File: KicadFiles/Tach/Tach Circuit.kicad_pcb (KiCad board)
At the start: 2 copper layers, 15 parts, among them Q1 2N3904

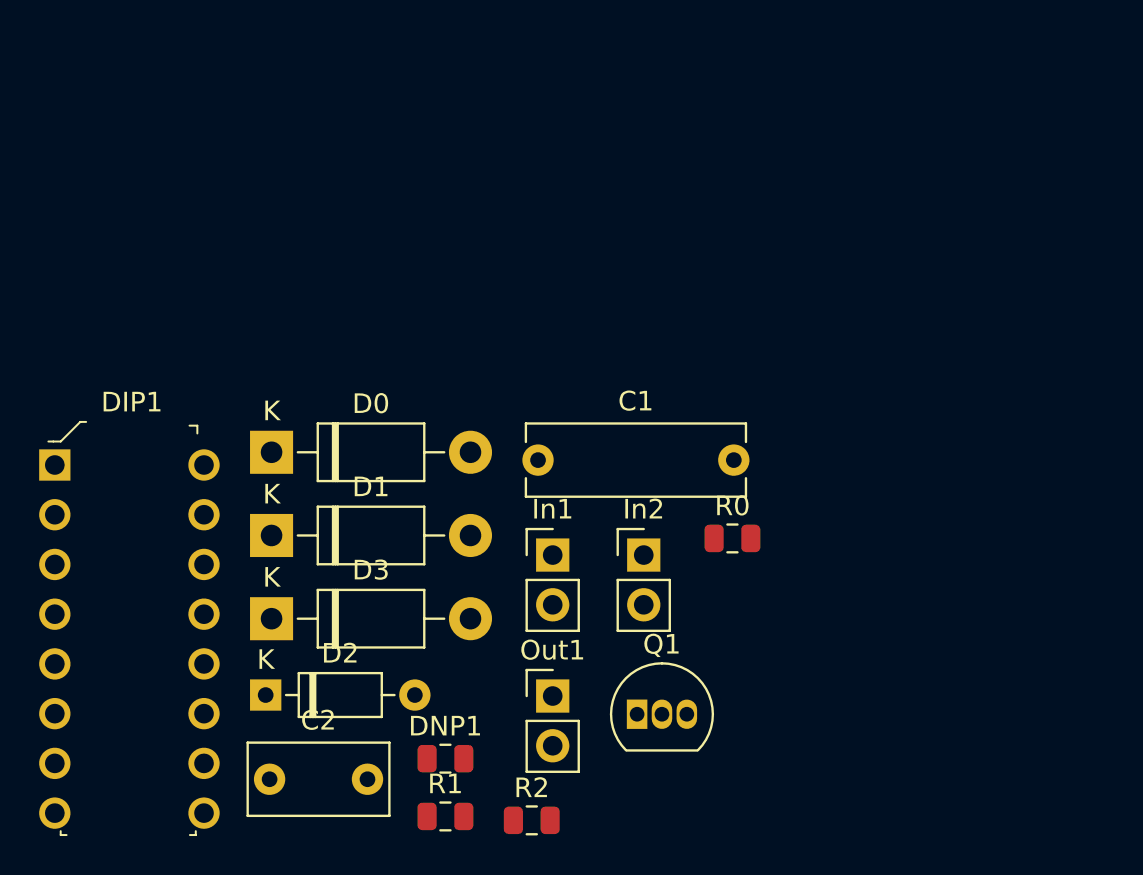
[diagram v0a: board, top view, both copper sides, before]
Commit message: ground = poured
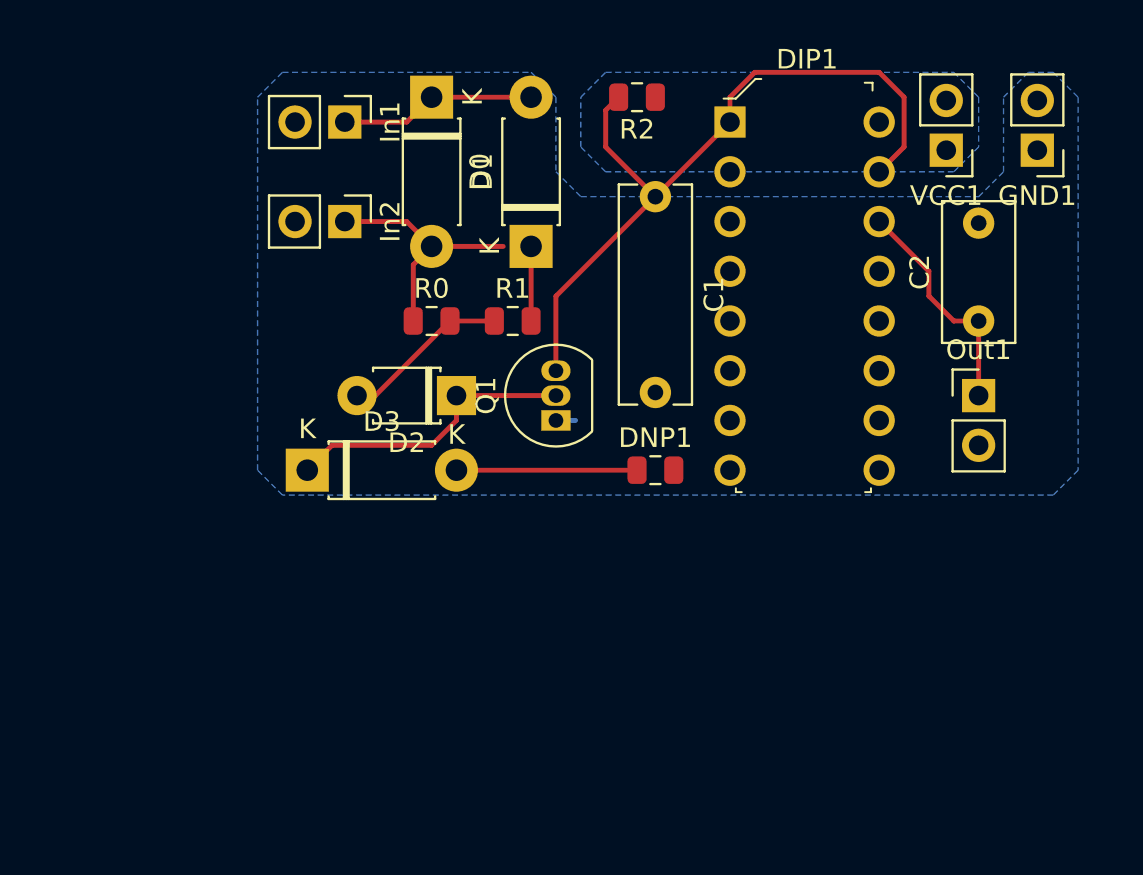
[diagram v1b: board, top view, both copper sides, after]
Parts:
- added GND1: GND, Connector_PinHeader_2.54mm:PinHeader_1x02_P2.54mm_Vertical, F.Cu at (164.3, -101.4)
- added VCC1: 5V, Connector_PinHeader_2.54mm:PinHeader_1x02_P2.54mm_Vertical, F.Cu at (159.6, -101.4)
- D0, D1, D3: footprint Diode_THT:D_DO-41_SOD81_P10.16mm_Horizontal -> Diode_THT:D_DO-41_SOD81_P7.62mm_Horizontal
- D2: footprint Diode_THT:D_DO-35_SOD27_P7.62mm_Horizontal -> Diode_THT:D_T-1_P5.08mm_Horizontal
- moved C2 43.1 mm to (161.3, -92.7), turned to 90 degrees
- moved DIP1 38.7 mm to (148.6, -102.9)
- moved R2 37.3 mm to (143.8, -104.1), turned to 180 degrees
- moved Out1 26.6 mm to (161.3, -88.9)
- moved R1 25.5 mm to (137.5, -92.7)
- moved In1 24.5 mm to (128.9, -102.9), turned to 270 degrees
- moved In2 22.9 mm to (128.9, -97.8), turned to 270 degrees
- moved D0 19.9 mm to (133.3, -104.1), turned to 270 degrees
- moved D1 19.8 mm to (138.4, -96.5), turned to 90 degrees
- moved R0 19.0 mm to (133.3, -92.7)
- moved DNP1 18.2 mm to (144.8, -85.1)
- moved D2 18.1 mm to (134.6, -88.9), turned to 180 degrees
- moved Q1 15.6 mm to (139.7, -87.6), turned to 90 degrees
- moved C1 14.7 mm to (144.8, -99.1), turned to 270 degrees
- moved D3 7.80 mm to (127.0, -85.1)
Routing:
- net Net-(C1-Pad1): track 0.00 -> 38.3 mm
- net Net-(D2-Pad1): track 0.00 -> 15.0 mm
- net Net-(D0-Pad2): track 0.00 -> 12.8 mm
- net Net-(C2-Pad1): track 0.00 -> 11.7 mm
- net Net-(D0-Pad1): track 0.00 -> 10.0 mm
- net Net-(D3-Pad2): track 0.00 -> 9.22 mm
- net Net-(D2-Pad2): track 0.00 -> 8.59 mm
- net Net-(D1-Pad1): track 0.00 -> 3.81 mm
- net GND: track 0.00 -> 1.37 mm
- added copper zone on B.Cu, net +5V
- added copper zone on B.Cu, net GND

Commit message: backdash footprints assigned
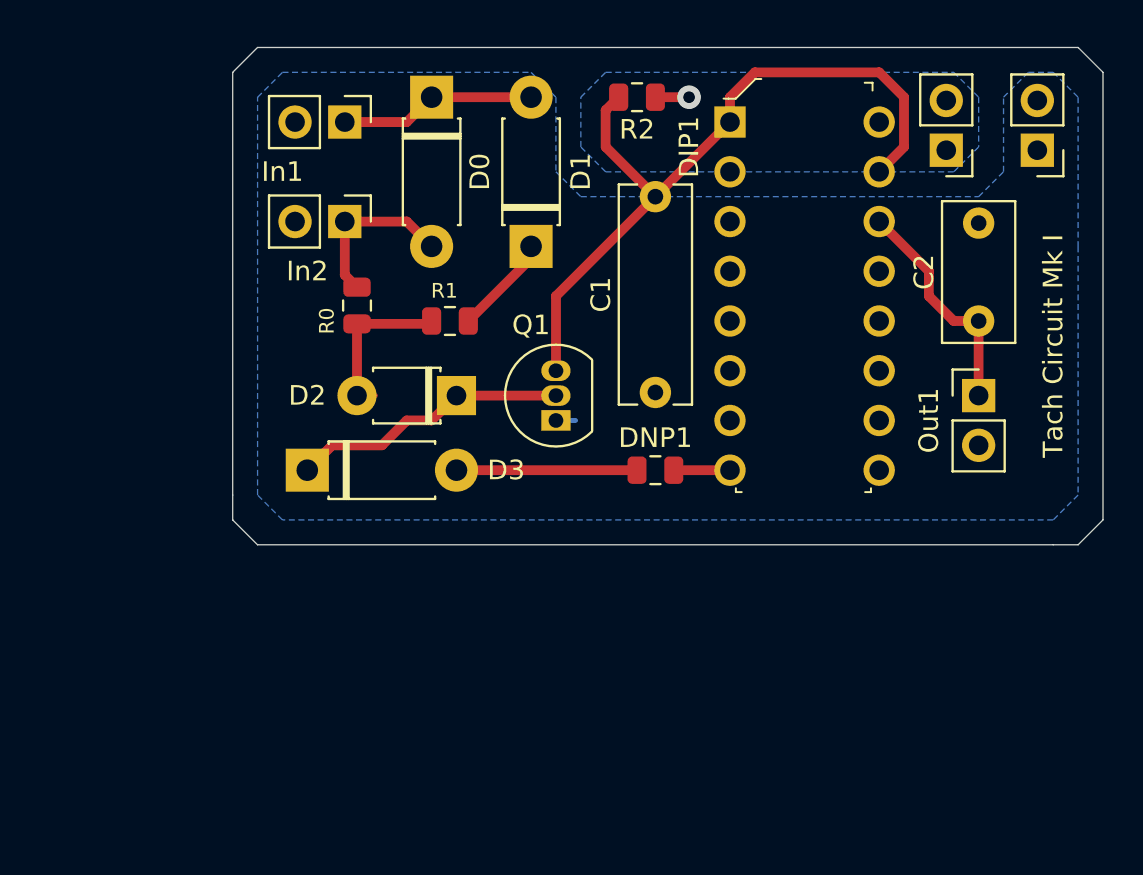
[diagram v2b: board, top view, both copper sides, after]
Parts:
- VCC1: value 5V -> +5V
- moved R0 3.89 mm to (129.5, -93.5), turned to 270 degrees
- moved R1 3.21 mm to (134.3, -92.7)
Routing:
- net Net-(D0-Pad2): track 12.8 -> 8.57 mm
- net GND: track 1.37 -> 4.25 mm
- net +5V: track 0.00 -> 1.72 mm, vias 0 -> 1
- net Net-(D1-Pad1): track 3.81 -> 5.14 mm
- net Net-(D2-Pad1): track 15.0 -> 14.3 mm
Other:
- board outline added: 44.4 x 25.4 mm
- board text added: "Tach Circuit Mk I"
